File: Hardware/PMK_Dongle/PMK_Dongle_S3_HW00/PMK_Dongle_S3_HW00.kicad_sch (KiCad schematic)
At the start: 26 parts, among them J10 USB_A, U20 MIC5528-3.3YMT-T5, U30 ESP32-S3FN8

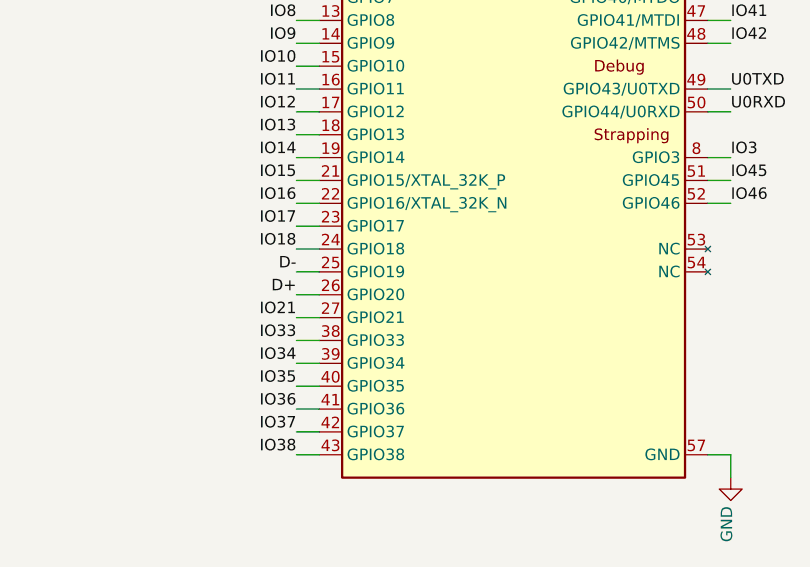
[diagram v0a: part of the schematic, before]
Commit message: started routing dongle_s3_00
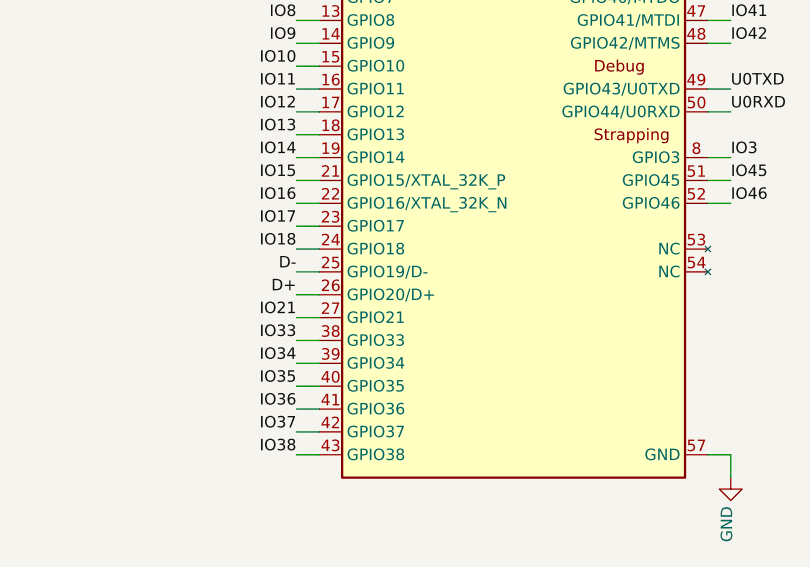
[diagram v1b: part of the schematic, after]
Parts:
- removed U30: ESP32-S3FN8, QFN40P700X700X90-57N-D, symbol Component_lib:ESP32-S3-PICO-1-N8R2
- added U30: ESP32-S3FN8, Component_lib:ESP32-S3-PICO-1-N8R2, symbol Component_lib:ESP32-S3-PICO-1-N8R2_sch
- C30: footprint (none) -> Capacitor_SMD:C_0603_1608Metric
- C31: footprint (none) -> Capacitor_SMD:C_0201_0603Metric
- R35: footprint (none) -> Resistor_SMD:R_0402_1005Metric
- TP30, TP31, TP32: footprint (none) -> Component_lib:TestPoint_0.8mm
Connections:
- net +3V3: now also U30.2 (VDD3P3_1), U30.20 (VDD3P3_RTC), U30.3 (VDD3P3_2), U30.46 (VDD3P3_CPU), U30.55 (VDDA_1), U30.56 (VDDA_2)
- net D+: now also U30.26 (GPIO20/D+)
- net D-: now also U30.25 (GPIO19/D-)
- net EN: now also U30.4 (CHIP_PU)
- net GND: now also U30.57 (GND)
- net IO0: now also U30.5 (GPIO0)
- net IO1: now also U30.6 (GPIO1)
- net IO10: now also U30.15 (GPIO10)
- net IO11: now also U30.16 (GPIO11)
- net IO12: now also U30.17 (GPIO12)
- net IO13: now also U30.18 (GPIO13)
- net IO14: now also U30.19 (GPIO14)
- net IO15: now also U30.21 (GPIO15/XTAL_32K_P)
- net IO16: now also U30.22 (GPIO16/XTAL_32K_N)
- net IO17: now also U30.23 (GPIO17)
- net IO18: now also U30.24 (GPIO18)
- net IO2: now also U30.7 (GPIO2)
- net IO21: now also U30.27 (GPIO21)
- net IO3: now also U30.8 (GPIO3)
- net IO33: now also U30.38 (GPIO33)
- net IO34: now also U30.39 (GPIO34)
- net IO35: now also U30.40 (GPIO35)
- net IO36: now also U30.41 (GPIO36)
- net IO37: now also U30.42 (GPIO37)
- net IO38: now also U30.43 (GPIO38)
- net IO39: now also U30.44 (GPIO39/MTCK)
- net IO4: now also U30.9 (GPIO4)
- net IO40: now also U30.45 (GPIO40/MTDO)
- net IO41: now also U30.47 (GPIO41/MTDI)
- net IO42: now also U30.48 (GPIO42/MTMS)
- net IO45: now also U30.51 (GPIO45)
- net IO46: now also U30.52 (GPIO46)
- net IO5: now also U30.10 (GPIO5)
- net IO6: now also U30.11 (GPIO6)
- net IO7: now also U30.12 (GPIO7)
- net IO8: now also U30.13 (GPIO8)
- net IO9: now also U30.14 (GPIO9)
- net LNA_IN: now also U30.1 (LNA_IN)
- net RX: now also U30.50 (GPIO44/U0RXD)
- net U0TXD: now also U30.49 (GPIO43/U0TXD)
